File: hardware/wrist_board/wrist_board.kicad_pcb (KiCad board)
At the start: 4 copper layers, 40 x 60 mm, 45 parts, among them J1 S2B-PH-K-S_LF__SN_, J2 USB_C_Receptacle_USB2.0_14P, J3 Conn_01x02, J4 Conn_01x02, J5 Conn_01x02, J6 Conn_01x02, J7 Conn_01x02, SW1 SW_SPST, U1 MCP73831T-2ACI_OT, U2 TLV75533PDBV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

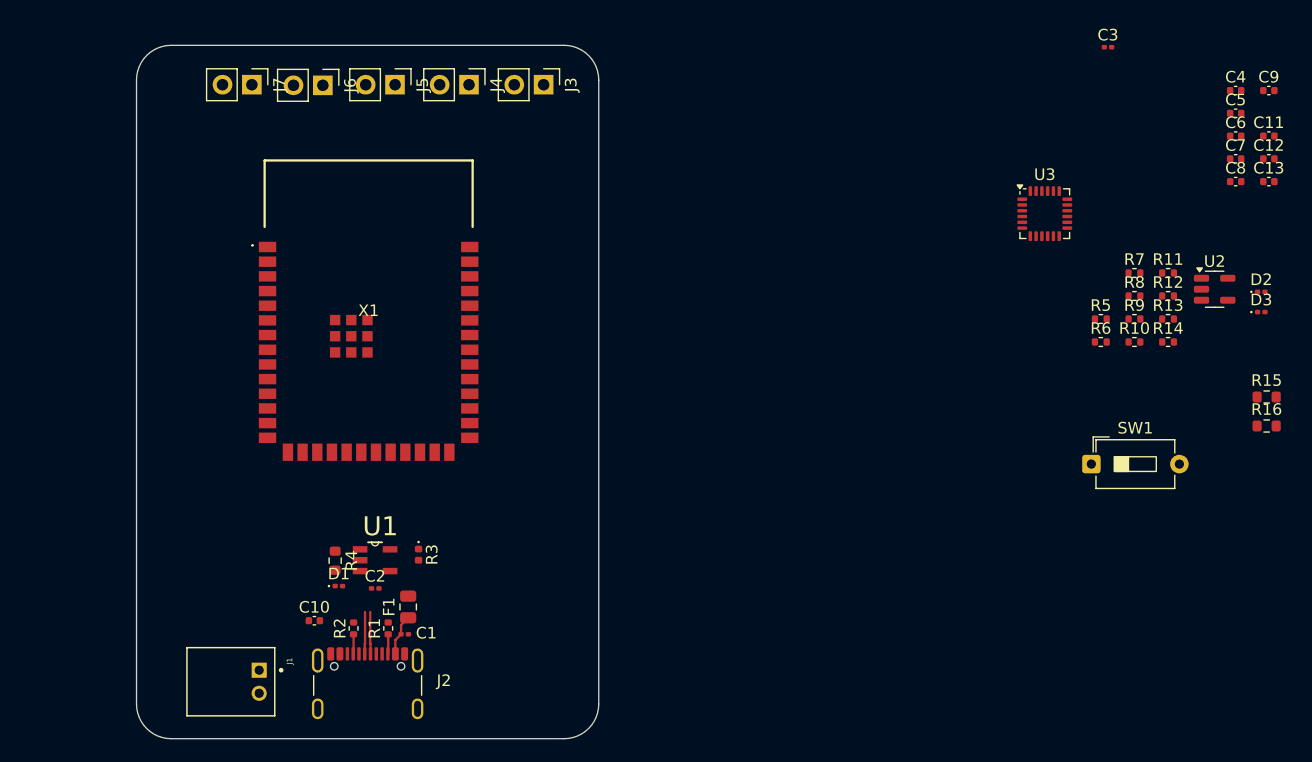
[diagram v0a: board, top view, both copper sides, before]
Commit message: New board orientation + USB/PWR routing
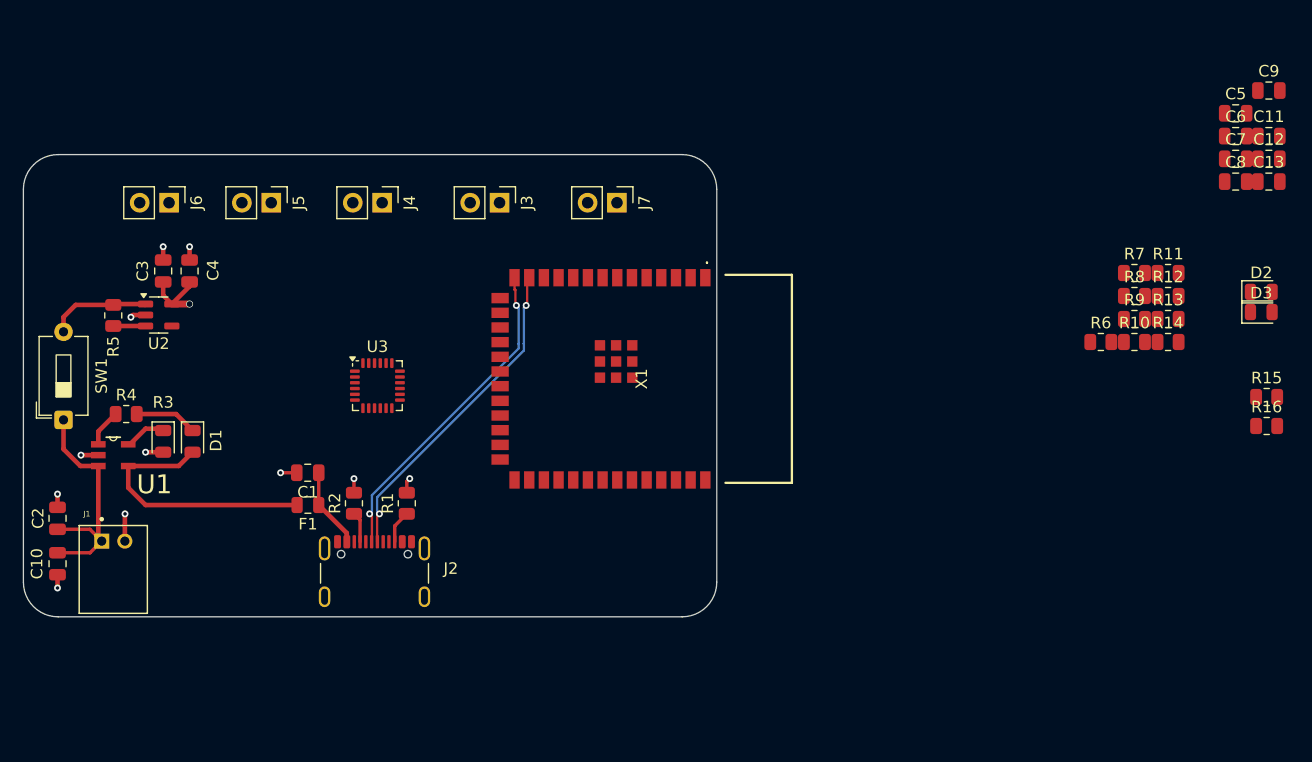
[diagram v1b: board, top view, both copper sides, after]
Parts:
- C1, C2, C3: footprint Capacitor_SMD:C_0201_0603Metric -> Capacitor_SMD:C_0805_2012Metric
- C10, C11, C12, C13, C4, C5, C6, C7, C8, C9: footprint Capacitor_SMD:C_0402_1005Metric -> Capacitor_SMD:C_0805_2012Metric
- D1, D2, D3: footprint LED_SMD:LED_0201_0603Metric -> LED_SMD:LED_0805_2012Metric
- R1, R10, R11, R12, R13, R14, R2, R5, R6, R7, R8, R9: footprint Resistor_SMD:R_0402_1005Metric -> Resistor_SMD:R_0805_2012Metric
- R15, R16, R4: footprint Resistor_SMD:R_0603_1608Metric -> Resistor_SMD:R_0805_2012Metric
- R3: footprint LED_SMD:LED_0402_1005Metric -> LED_SMD:LED_0805_2012Metric
- moved C4 91.9 mm to (80.5, 97.3), turned to 90 degrees
- moved U2 91.4 mm to (77.8, 101.2)
- moved SW1 89.0 mm to (69.6, 110.2), turned to 90 degrees
- moved R5 85.5 mm to (73.9, 101.2), turned to -90 degrees
- moved C3 84.0 mm to (78.2, 97.3), turned to 90 degrees
- moved U3 59.6 mm to (96.8, 107.3)
- moved J7 33.2 mm to (117.5, 91.4)
- moved C2 28.2 mm to (69.1, 118.8), turned to 90 degrees
- moved X1 24.7 mm to (119.9, 106.7), turned to -90 degrees
- moved U1 24.4 mm to (73.9, 113.3)
- moved R3 24.2 mm to (78.2, 112.1)
- moved C10 22.8 mm to (69.1, 122.7), turned to -90 degrees
- moved R4 22.1 mm to (75.0, 109.7), turned to 0 degrees
- moved D1 17.8 mm to (80.8, 112.1), turned to -90 degrees
- moved J1 17.5 mm to (73.9, 120.7), turned to 0 degrees
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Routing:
- net /D-: track 3.64 -> 28.5 mm, vias 0 -> 2
- net /D+: track 3.64 -> 28.5 mm, vias 0 -> 2
- net +5V: track 0.00 -> 23.2 mm
- net /<NO NET>: track 0.00 -> 21.3 mm
- net GND: track 0.00 -> 15.3 mm, vias 0 -> 11
- net Net-(SW1-B): track 0.00 -> 8.95 mm
- net +3V3: track 0.00 -> 6.30 mm, vias 0 -> 1
- net Net-(D1-K): track 0.00 -> 5.42 mm
- net Net-(U1-PROG): track 0.00 -> 3.65 mm
- net Net-(C1-Pad1): track 3.58 -> 6.98 mm
- net Net-(U1-STAT): track 0.00 -> 3.24 mm
- net Net-(U2-EN): track 0.00 -> 2.79 mm
- net Net-(J2-CC2): track 1.71 -> 2.85 mm
- net Net-(J2-CC1): track 1.71 -> 2.63 mm
- added copper zone on In2.Cu, net +3V3
- added copper zone on In1.Cu, net GND
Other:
- board size 40 x 60 mm -> 60 x 40 mm
